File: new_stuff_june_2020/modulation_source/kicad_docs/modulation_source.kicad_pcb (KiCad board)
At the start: 2 copper layers, 99.1 x 68.6 mm, 72 parts, among them J1 power_in, Q1 BC560, Q2 BC560, Q3 BF245A, Q4 BC550, Q5 BC550, Q6 BC550, U1 LM13700, U2 TL072, U3 TL072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

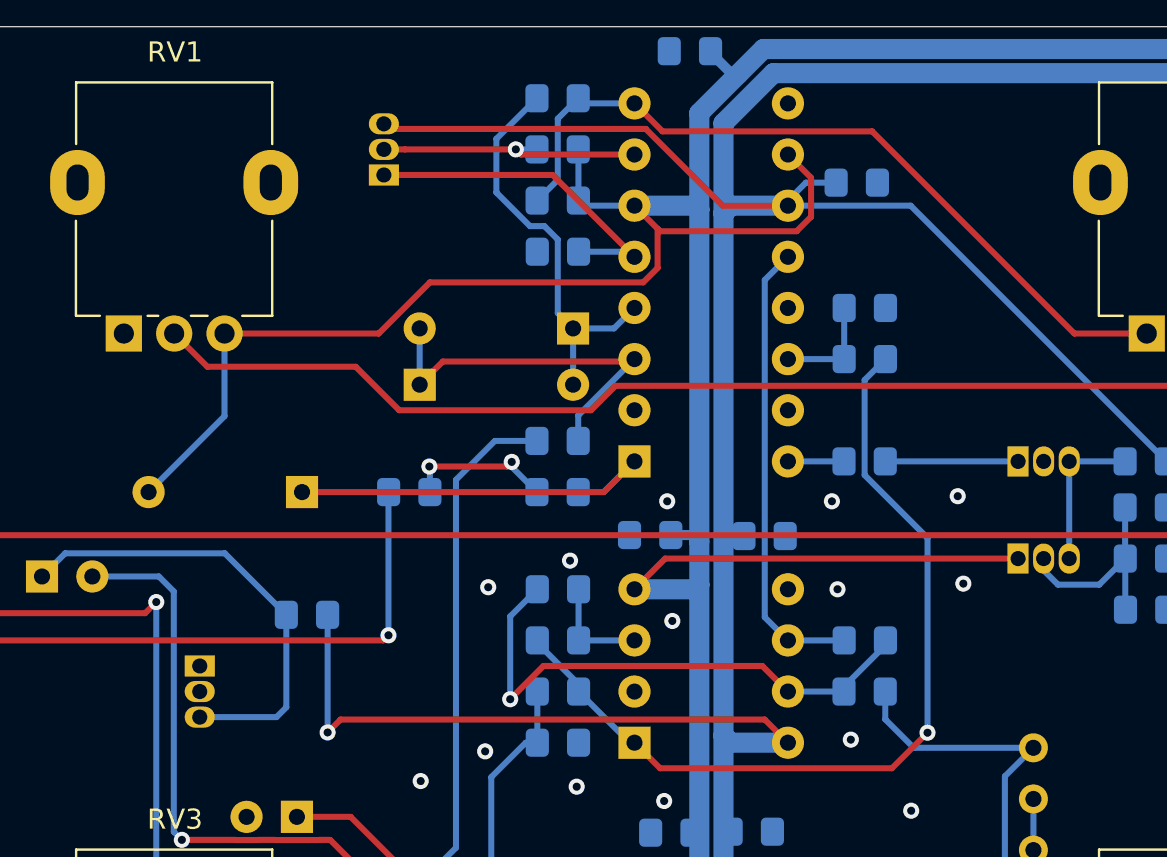
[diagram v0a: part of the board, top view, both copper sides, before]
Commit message: change modulation-source fm circuit, make new gerbers
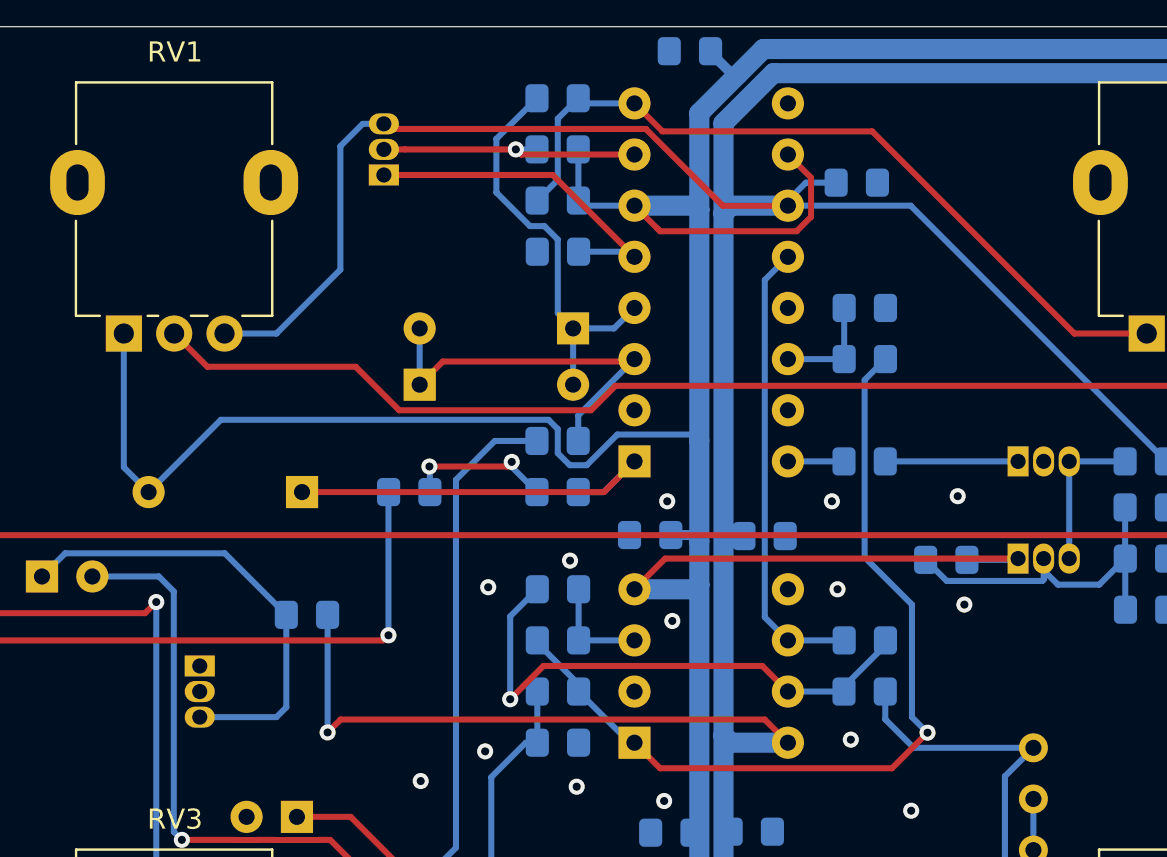
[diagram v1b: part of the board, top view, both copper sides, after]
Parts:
- added R34: ???, Resistor_SMD:R_0805_2012Metric_Pad1.15x1.40mm_HandSolder, B.Cu at (164.1, 77.3)
- R4: value 100k -> 180k
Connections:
- RV1 pad 1: GND -> -12V
- RV1 pad 3: -12V -> +12V
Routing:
- net +12V: track 238.9 -> 254.7 mm
- net -12V: track 251.8 -> 259.7 mm
- net Net-(Q1-Pad2): track 10.6 -> 17.9 mm

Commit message: update values to scale frequency and noise level
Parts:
- R2: value 300k -> 200k
- R34: value ??? -> 220k
- R4: value 180k -> 270k
- R5: value 33k -> 100k
- R6, R9: value ??? -> 2k
- RV6: value ??? -> 1k
